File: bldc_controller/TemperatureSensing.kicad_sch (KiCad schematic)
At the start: 9 parts

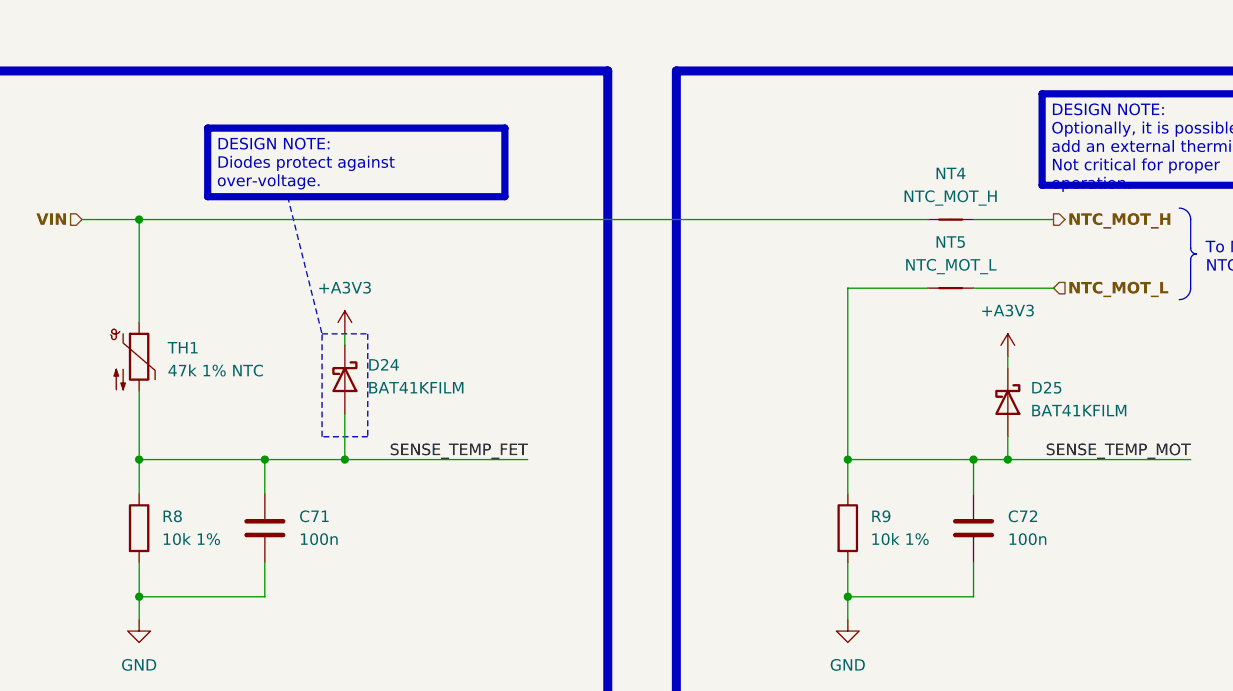
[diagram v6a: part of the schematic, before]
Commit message: routed all signals. TODO: redo all power polygons and ensure good return paths/reference. Added 3d models
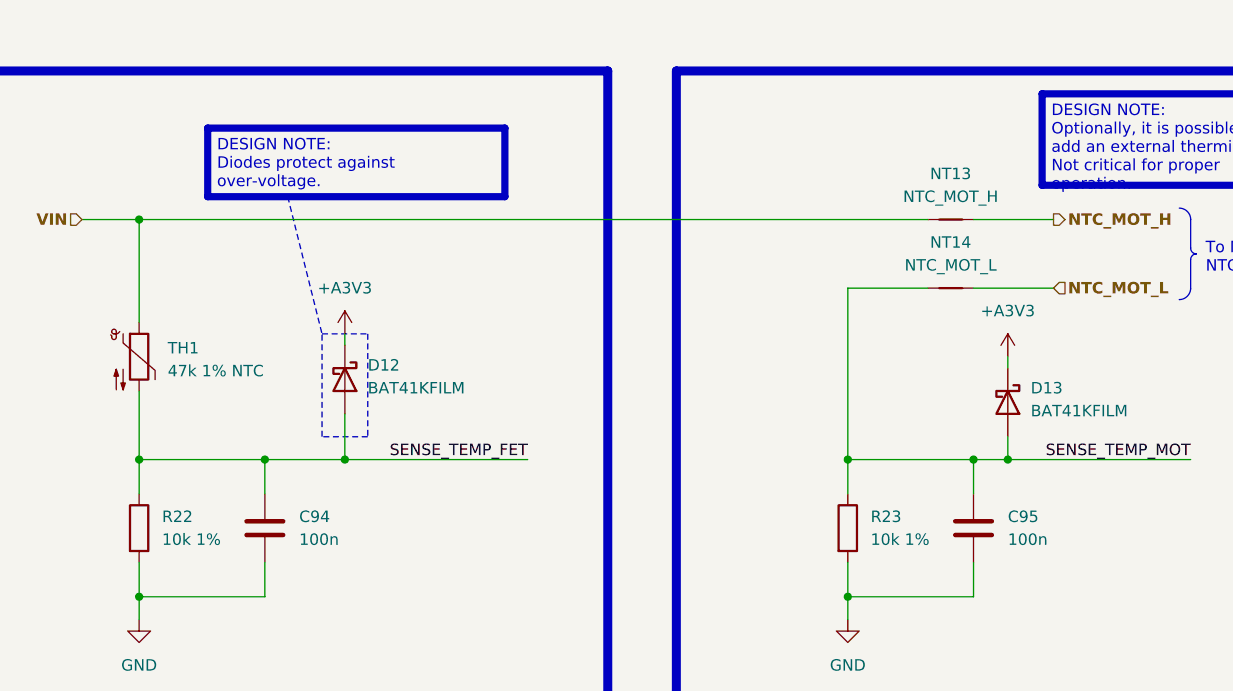
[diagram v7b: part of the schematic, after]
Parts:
- renumbered C71 to C94, C72 to C95, D24 to D12, D25 to D13, NT4 to NT13, NT5 to NT14, R8 to R22, R9 to R23
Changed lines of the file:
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@@
   (symbol (lib_id "Device:NetTie_2") (at 187.96 67.31 0) (unit 1)
     (in_bom no) (on_board yes) (dnp no) (fields_autoplaced)
-    (property "Reference" "NT4" (at 187.96 62.23 0)
+    (property "Reference" "NT13" (at 187.96 62.23 0)
       (effects (font (size 1.27 1.27)))
     )
@@
       (project "bldc_controller"
         (path "/0650c7a8-acba-429c-9f8e-eec0baf0bc1c/fede4c36-00cc-4d3d-b71c-5243ba232202/fa34585c-cea0-4980-9405-23c394490fcf"
-          (reference "NT4") (unit 1)
+          (reference "NT13") (unit 1)
         )
       )
@@
   (symbol (lib_id "0_diode:BAT41KFILM") (at 120.65 85.09 270) (unit 1)
     (in_bom yes) (on_board yes) (dnp no) (fields_autoplaced)
-    (property "Reference" "D24" (at 123.19 83.5025 90)
+    (property "Reference" "D12" (at 123.19 83.5025 90)
       (effects (font (size 1.27 1.27)) (justify left))
     )
@@
       (project "bldc_controller"
         (path "/0650c7a8-acba-429c-9f8e-eec0baf0bc1c/fede4c36-00cc-4d3d-b71c-5243ba232202/fa34585c-cea0-4980-9405-23c394490fcf"
-          (reference "D24") (unit 1)
+          (reference "D12") (unit 1)
         )
       )
@@
   (symbol (lib_id "power:GND") (at 176.53 111.76 0) (unit 1)
     (in_bom yes) (on_board yes) (dnp no) (fields_autoplaced)
-    (property "Reference" "#PWR063" (at 176.53 118.11 0)
+    (property "Reference" "#PWR042" (at 176.53 118.11 0)
       (effects (font (size 1.27 1.27)) hide)
     )
@@
       (project "bldc_controller"
         (path "/0650c7a8-acba-429c-9f8e-eec0baf0bc1c/fede4c36-00cc-4d3d-b71c-5243ba232202/fa34585c-cea0-4980-9405-23c394490fcf"
-          (reference "#PWR063") (unit 1)
+          (reference "#PWR042") (unit 1)
         )
       )
@@
   (symbol (lib_id "Device:R") (at 97.79 101.6 0) (unit 1)
     (in_bom yes) (on_board yes) (dnp no) (fields_autoplaced)
-    (property "Reference" "R8" (at 100.33 100.33 0)
+    (property "Reference" "R22" (at 100.33 100.33 0)
       (effects (font (size 1.27 1.27)) (justify left))
     )
@@
       (project "bldc_controller"
         (path "/0650c7a8-acba-429c-9f8e-eec0baf0bc1c/fede4c36-00cc-4d3d-b71c-5243ba232202/fa34585c-cea0-4980-9405-23c394490fcf"
-          (reference "R8") (unit 1)
+          (reference "R22") (unit 1)
         )
       )
@@
         )
         (path "/0650c7a8-acba-429c-9f8e-eec0baf0bc1c/fede4c36-00cc-4d3d-b71c-5243ba232202/fa34585c-cea0-4980-9405-23c394490fcf"
-          (reference "#PWR064") (unit 1)
+          (reference "#PWR043") (unit 1)
         )
       )
@@
   (symbol (lib_id "Device:R") (at 176.53 101.6 0) (unit 1)
     (in_bom yes) (on_board yes) (dnp no) (fields_autoplaced)
-    (property "Reference" "R9" (at 179.07 100.33 0)
+    (property "Reference" "R23" (at 179.07 100.33 0)
       (effects (font (size 1.27 1.27)) (justify left))
     )
@@
       (project "bldc_controller"
         (path "/0650c7a8-acba-429c-9f8e-eec0baf0bc1c/fede4c36-00cc-4d3d-b71c-5243ba232202/fa34585c-cea0-4980-9405-23c394490fcf"
-          (reference "R9") (unit 1)
+          (reference "R23") (unit 1)
         )
       )
@@
   (symbol (lib_id "0_diode:BAT41KFILM") (at 194.31 87.63 270) (unit 1)
     (in_bom yes) (on_board yes) (dnp no) (fields_autoplaced)
-    (property "Reference" "D25" (at 196.85 86.0425 90)
+    (property "Reference" "D13" (at 196.85 86.0425 90)
       (effects (font (size 1.27 1.27)) (justify left))
     )
@@
       (project "bldc_controller"
         (path "/0650c7a8-acba-429c-9f8e-eec0baf0bc1c/fede4c36-00cc-4d3d-b71c-5243ba232202/fa34585c-cea0-4980-9405-23c394490fcf"
-          (reference "D25") (unit 1)
+          (reference "D13") (unit 1)
         )
       )
@@
   (symbol (lib_id "Device:C") (at 111.76 101.6 0) (unit 1)
     (in_bom yes) (on_board yes) (dnp no) (fields_autoplaced)
-    (property "Reference" "C71" (at 115.57 100.33 0)
+    (property "Reference" "C94" (at 115.57 100.33 0)
       (effects (font (size 1.27 1.27)) (justify left))
     )
@@
       (project "bldc_controller"
         (path "/0650c7a8-acba-429c-9f8e-eec0baf0bc1c/fede4c36-00cc-4d3d-b71c-5243ba232202/fa34585c-cea0-4980-9405-23c394490fcf"
-          (reference "C71") (unit 1)
+          (reference "C94") (unit 1)
         )
       )
@@
   (symbol (lib_id "power:GND") (at 97.79 111.76 0) (unit 1)
     (in_bom yes) (on_board yes) (dnp no) (fields_autoplaced)
-    (property "Reference" "#PWR061" (at 97.79 118.11 0)
+    (property "Reference" "#PWR040" (at 97.79 118.11 0)
       (effects (font (size 1.27 1.27)) hide)
     )
@@
       (project "bldc_controller"
         (path "/0650c7a8-acba-429c-9f8e-eec0baf0bc1c/fede4c36-00cc-4d3d-b71c-5243ba232202/fa34585c-cea0-4980-9405-23c394490fcf"
-          (reference "#PWR061") (unit 1)
+          (reference "#PWR040") (unit 1)
         )
       )
@@
         )
         (path "/0650c7a8-acba-429c-9f8e-eec0baf0bc1c/fede4c36-00cc-4d3d-b71c-5243ba232202/fa34585c-cea0-4980-9405-23c394490fcf"
-          (reference "#PWR062") (unit 1)
+          (reference "#PWR041") (unit 1)
         )
       )
@@
   (symbol (lib_id "Device:NetTie_2") (at 187.96 74.93 0) (unit 1)
     (in_bom no) (on_board yes) (dnp no)
-    (property "Reference" "NT5" (at 187.96 69.85 0)
+    (property "Reference" "NT14" (at 187.96 69.85 0)
       (effects (font (size 1.27 1.27)))
     )
@@
       (project "bldc_controller"
         (path "/0650c7a8-acba-429c-9f8e-eec0baf0bc1c/fede4c36-00cc-4d3d-b71c-5243ba232202/fa34585c-cea0-4980-9405-23c394490fcf"
-          (reference "NT5") (unit 1)
+          (reference "NT14") (unit 1)
         )
       )
@@
   (symbol (lib_id "Device:C") (at 190.5 101.6 0) (unit 1)
     (in_bom yes) (on_board yes) (dnp no) (fields_autoplaced)
-    (property "Reference" "C72" (at 194.31 100.33 0)
+    (property "Reference" "C95" (at 194.31 100.33 0)
       (effects (font (size 1.27 1.27)) (justify left))
     )
@@
       (project "bldc_controller"
         (path "/0650c7a8-acba-429c-9f8e-eec0baf0bc1c/fede4c36-00cc-4d3d-b71c-5243ba232202/fa34585c-cea0-4980-9405-23c394490fcf"
-          (reference "C72") (unit 1)
-        )
-      )
+          (reference "C95") (unit 1)
+        )
+      )

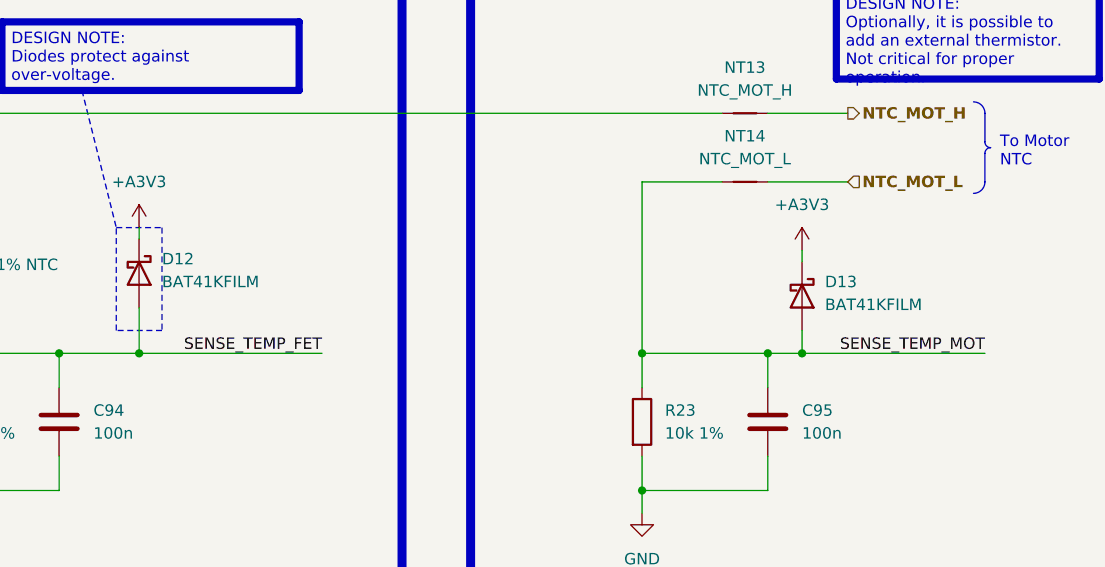
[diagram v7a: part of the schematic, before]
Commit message: started routing polygons
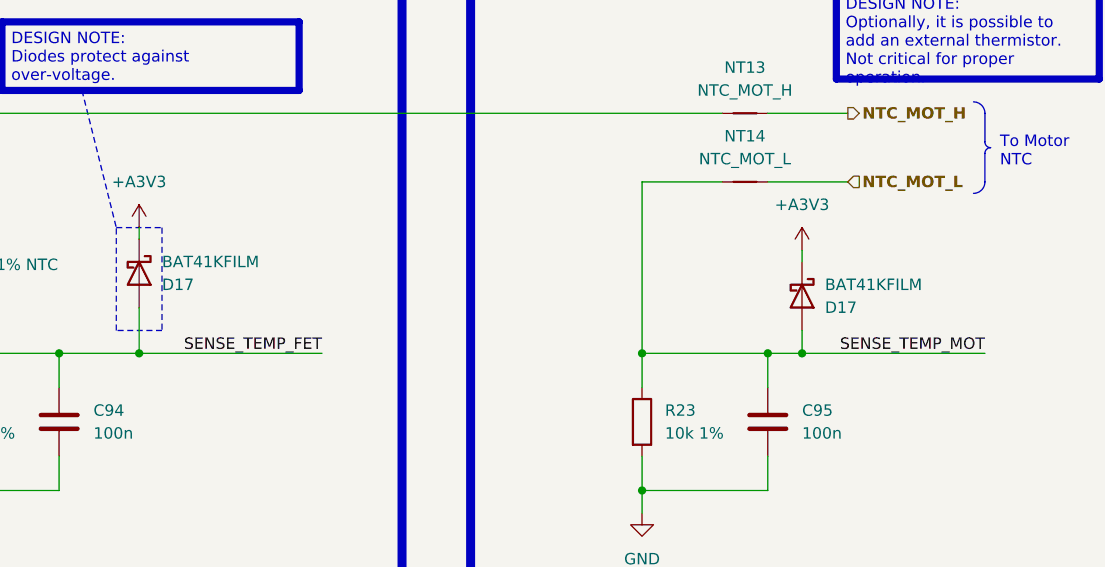
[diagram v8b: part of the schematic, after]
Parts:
- removed D12, D13: BAT41KFILM, Diode_SMD:D_SOD-523, symbol 0_diode:BAT41KFILM
- added D17 (x2): BAT41KFILM, 0_diode_smd:D_SOD-523, symbol 0_diode:BAT41KFILM
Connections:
- net +A3V3: now also D17.1 (K), D17.1 (K)
- net SENSE_TEMP_FET: now also D17.2 (A)
- net SENSE_TEMP_MOT: now also D17.2 (A)
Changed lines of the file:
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@@
-    )
-  )
-  (symbol (lib_id "0_diode:BAT41KFILM") (at 120.65 85.09 270) (unit 1)
-    (in_bom yes) (on_board yes) (dnp no) (fields_autoplaced)
-    (property "Reference" "D12" (at 123.19 83.5025 90)
-      (effects (font (size 1.27 1.27)) (justify left))
-    )
-    (property "Value" "BAT41KFILM" (at 123.19 86.0425 90)
-      (effects (font (size 1.27 1.27)) (justify left))
-    )
-    (property "Footprint" "Diode_SMD:D_SOD-523" (at 116.205 85.09 0)
-      (effects (font (size 1.27 1.27)) hide)
-    )
-    (property "Datasheet" "https://www.mouser.ch/datasheet/2/389/bat41-1848934.pdf" (at 120.65 85.09 0)
-      (effects (font (size 1.27 1.27)) hide)
-    )
-    (pin "1")
-    (pin "2")
-    (instances
-      (project "bldc_controller"
-        (path "/0650c7a8-acba-429c-9f8e-eec0baf0bc1c/fede4c36-00cc-4d3d-b71c-5243ba232202/fa34585c-cea0-4980-9405-23c394490fcf"
-          (reference "D12") (unit 1)
-        )
-      )
     )
   )
@@
     )
   )
-  (symbol (lib_id "0_diode:BAT41KFILM") (at 194.31 87.63 270) (unit 1)
-    (in_bom yes) (on_board yes) (dnp no) (fields_autoplaced)
-    (property "Reference" "D13" (at 196.85 86.0425 90)
-      (effects (font (size 1.27 1.27)) (justify left))
-    )
-    (property "Value" "BAT41KFILM" (at 196.85 88.5825 90)
-      (effects (font (size 1.27 1.27)) (justify left))
-    )
-    (property "Footprint" "Diode_SMD:D_SOD-523" (at 189.865 87.63 0)
-      (effects (font (size 1.27 1.27)) hide)
-    )
-    (property "Datasheet" "https://www.mouser.ch/datasheet/2/389/bat41-1848934.pdf" (at 194.31 87.63 0)
-      (effects (font (size 1.27 1.27)) hide)
-    )
-    (pin "1")
-    (pin "2")
-    (instances
-      (project "bldc_controller"
-        (path "/0650c7a8-acba-429c-9f8e-eec0baf0bc1c/fede4c36-00cc-4d3d-b71c-5243ba232202/fa34585c-cea0-4980-9405-23c394490fcf"
-          (reference "D13") (unit 1)
-        )
-      )
-    )
-  )
   (symbol (lib_id "Device:C") (at 111.76 101.6 0) (unit 1)
     (in_bom yes) (on_board yes) (dnp no) (fields_autoplaced)
@@
         (path "/0650c7a8-acba-429c-9f8e-eec0baf0bc1c/fede4c36-00cc-4d3d-b71c-5243ba232202/fa34585c-cea0-4980-9405-23c394490fcf"
           (reference "C94") (unit 1)
+        )
+      )
+    )
+  )
+  (symbol (lib_name "BAT41KFILM_1") (lib_id "0_diode:BAT41KFILM") (at 194.31 87.63 270) (unit 1)
+    (in_bom yes) (on_board yes) (dnp no)
+    (property "Reference" "D17" (at 196.85 88.9 90)
+      (effects (font (size 1.27 1.27)) (justify left))
+    )
+    (property "Value" "BAT41KFILM" (at 196.85 86.36 90)
+      (effects (font (size 1.27 1.27)) (justify left))
+    )
+    (property "Footprint" "0_diode_smd:D_SOD-523" (at 189.865 87.63 0)
+      (effects (font (size 1.27 1.27)) hide)
+    )
+    (property "Datasheet" "https://www.mouser.ch/datasheet/2/389/bat41-1848934.pdf" (at 194.31 87.63 0)
+      (effects (font (size 1.27 1.27)) hide)
+    )
+    (pin "1")
+    (pin "2")
+    (instances
+      (project "bldc_controller"
+        (path "/0650c7a8-acba-429c-9f8e-eec0baf0bc1c/fede4c36-00cc-4d3d-b71c-5243ba232202/d359abe5-ae6a-4888-8140-3e6566d20c15"
+          (reference "D17") (unit 1)
+        )
+        (path "/0650c7a8-acba-429c-9f8e-eec0baf0bc1c/fede4c36-00cc-4d3d-b71c-5243ba232202/fa34585c-cea0-4980-9405-23c394490fcf"
+          (reference "D13") (unit 1)
         )
       )
@@
         )
       )
+    )
+  )
+  (symbol (lib_name "BAT41KFILM_1") (lib_id "0_diode:BAT41KFILM") (at 120.65 85.09 270) (unit 1)
+    (in_bom yes) (on_board yes) (dnp no)
+    (property "Reference" "D17" (at 123.19 86.36 90)
+      (effects (font (size 1.27 1.27)) (justify left))
+    )
+    (property "Value" "BAT41KFILM" (at 123.19 83.82 90)
+      (effects (font (size 1.27 1.27)) (justify left))
+    )
+    (property "Footprint" "0_diode_smd:D_SOD-523" (at 116.205 85.09 0)
+      (effects (font (size 1.27 1.27)) hide)
+    )
+    (property "Datasheet" "https://www.mouser.ch/datasheet/2/389/bat41-1848934.pdf" (at 120.65 85.09 0)
+      (effects (font (size 1.27 1.27)) hide)
+    )
+    (pin "1")
+    (pin "2")
+    (instances
+      (project "bldc_controller"
+        (path "/0650c7a8-acba-429c-9f8e-eec0baf0bc1c/fede4c36-00cc-4d3d-b71c-5243ba232202/d359abe5-ae6a-4888-8140-3e6566d20c15"
+          (reference "D17") (unit 1)
+        )
+        (path "/0650c7a8-acba-429c-9f8e-eec0baf0bc1c/fede4c36-00cc-4d3d-b71c-5243ba232202/fa34585c-cea0-4980-9405-23c394490fcf"
+          (reference "D12") (unit 1)
+        )
+      )
